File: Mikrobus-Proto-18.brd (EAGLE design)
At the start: 27.9 x 57.1 mm, 38 parts

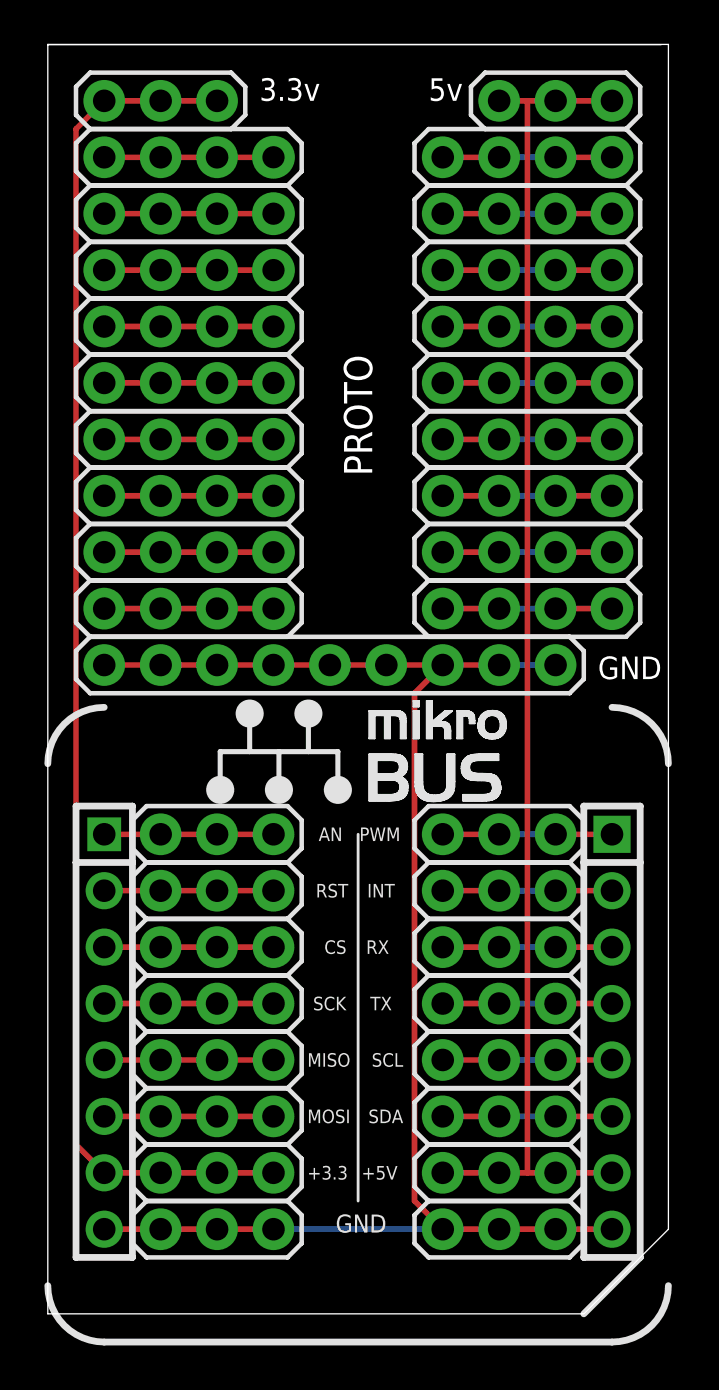
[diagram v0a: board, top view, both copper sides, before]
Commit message: Add Ground Plane
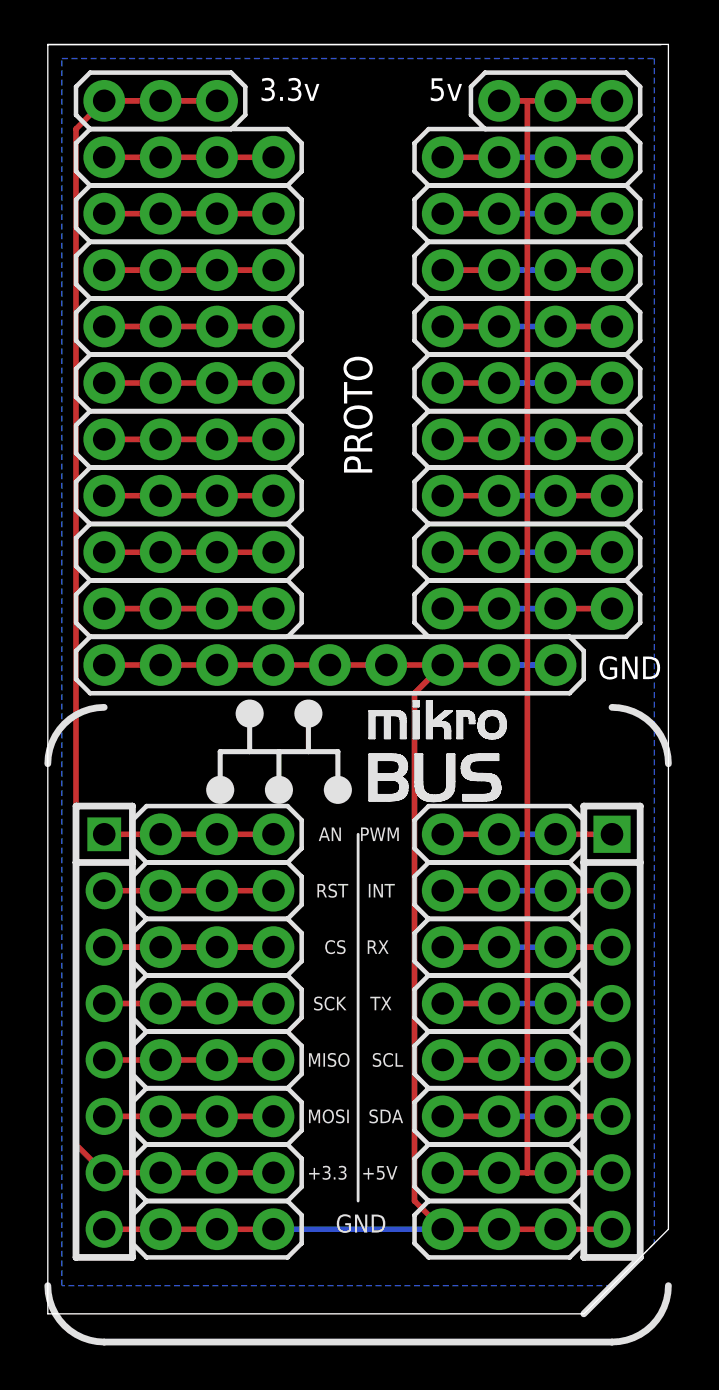
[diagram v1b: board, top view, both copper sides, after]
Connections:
- removed net N$21: JP8.1, JP8.2, JP8.3, JP9.1, JP9.2, JP9.3, MB1.8, MB1.9, U$3.1, U$3.2, U$3.3, U$3.4, U$3.5, U$3.6, U$3.7, U$3.8, U$3.9
- removed net N$46: U$18.1, U$18.2, U$18.3, U$18.4
- new net GND: JP8.1, JP8.2, JP8.3, JP9.1, JP9.2, JP9.3, MB1.8, MB1.9, U$18.1, U$18.2, U$18.3, U$18.4, U$3.1, U$3.2, U$3.3, U$3.4, U$3.5, U$3.6, U$3.7, U$3.8, U$3.9
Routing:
- net GND: track 0.00 -> 77.3 mm
- net N$21: track 69.6 -> 0.00 mm
- net N$46: track 7.62 -> 0.00 mm
- added copper zone on layer 16, net GND

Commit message: Signal names changed for preperation of Fritzing parts
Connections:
- net N$1 renamed INT
- net N$11 renamed MISO
- net N$13 renamed AN
- net N$15 renamed MOSI
- net N$2 renamed +5V
- net N$24 renamed PWM
- net N$26 renamed TX
- net N$29 renamed RX
- net N$32 renamed SDA
- net N$35 renamed SCL
- net N$4 renamed +3.3V
- net N$43 renamed RST
- net N$48 renamed SCK
- net N$5 renamed CS
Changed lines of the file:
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@@
 </elements>
 <signals>
-<signal name="N$13">
+<signal name="AN">
 <contactref element="JP1" pad="3"/>
 <contactref element="MB1" pad="1"/>
@@
 <wire x1="7.62" y1="22.86" x2="5.08" y2="22.86" width="0.254" layer="1"/>
 </signal>
-<signal name="N$1">
+<signal name="INT">
 <contactref element="JP16" pad="1"/>
 <contactref element="MB1" pad="15"/>
@@
 <wire x1="20.32" y1="20.32" x2="22.86" y2="20.32" width="0.254" layer="16"/>
 </signal>
-<signal name="N$5">
+<signal name="CS">
 <contactref element="JP3" pad="2"/>
 <contactref element="JP3" pad="1"/>
@@
 <wire x1="7.62" y1="17.78" x2="10.16" y2="17.78" width="0.254" layer="1"/>
 </signal>
-<signal name="N$11">
+<signal name="MISO">
 <contactref element="JP5" pad="2"/>
 <contactref element="JP5" pad="1"/>
@@
 <wire x1="7.62" y1="12.7" x2="10.16" y2="12.7" width="0.254" layer="1"/>
 </signal>
-<signal name="N$15">
+<signal name="MOSI">
 <contactref element="JP6" pad="2"/>
 <contactref element="JP6" pad="1"/>
@@
 <wire x1="7.62" y1="10.16" x2="10.16" y2="10.16" width="0.254" layer="1"/>
 </signal>
-<signal name="N$24">
+<signal name="PWM">
 <contactref element="JP15" pad="2"/>
 <contactref element="MB1" pad="16"/>
@@
 <wire x1="20.32" y1="22.86" x2="22.86" y2="22.86" width="0.254" layer="16"/>
 </signal>
-<signal name="N$26">
+<signal name="TX">
 <contactref element="JP13" pad="1"/>
 <contactref element="MB1" pad="13"/>
@@
 <wire x1="20.32" y1="15.24" x2="22.86" y2="15.24" width="0.254" layer="16"/>
 </signal>
-<signal name="N$29">
+<signal name="RX">
 <contactref element="JP14" pad="1"/>
 <contactref element="MB1" pad="14"/>
@@
 <wire x1="20.32" y1="17.78" x2="22.86" y2="17.78" width="0.254" layer="16"/>
 </signal>
-<signal name="N$32">
+<signal name="SDA">
 <contactref element="JP11" pad="1"/>
 <contactref element="MB1" pad="11"/>
@@
 <wire x1="20.32" y1="10.16" x2="22.86" y2="10.16" width="0.254" layer="16"/>
 </signal>
-<signal name="N$35">
+<signal name="SCL">
 <contactref element="JP12" pad="1"/>
 <contactref element="MB1" pad="12"/>
@@
 <wire x1="20.32" y1="12.7" x2="22.86" y2="12.7" width="0.254" layer="16"/>
 </signal>
-<signal name="N$4">
+<signal name="+3.3V">
 <contactref element="JP7" pad="1"/>
 <contactref element="JP17" pad="3"/>
@@
 <wire x1="22.86" y1="53.34" x2="20.32" y2="53.34" width="0.254" layer="16"/>
 </signal>
-<signal name="N$43">
+<signal name="RST">
 <contactref element="JP2" pad="1"/>
 <contactref element="JP2" pad="2"/>
@@
 <wire x1="7.62" y1="20.32" x2="10.16" y2="20.32" width="0.254" layer="1"/>
 </signal>
-<signal name="N$48">
+<signal name="SCK">
 <contactref element="JP4" pad="1"/>
 <contactref element="JP4" pad="2"/>
@@
 <wire x1="7.62" y1="15.24" x2="10.16" y2="15.24" width="0.254" layer="1"/>
 </signal>
-<signal name="N$2">
+<signal name="+5V">
 <contactref element="JP10" pad="1"/>
 <contactref element="MB1" pad="10"/>

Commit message: Better Fritzing part thanks to Steve Lilley
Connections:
- net N$12 renamed R8
- net N$16 renamed L7
- net N$17 renamed R7
- net N$19 renamed L6
- net N$20 renamed R6
- net N$22 renamed R9
- net N$25 renamed L8
- net N$28 renamed L5
- net N$31 renamed R5
- net N$34 renamed L4
- net N$37 renamed R4
- net N$38 renamed L3
- net N$40 renamed R3
- net N$44 renamed L2
- net N$45 renamed R2
- net N$47 renamed R1
- net N$9 renamed L9
- new net L1: U$18.1, U$18.2, U$18.3, U$18.4
- net GND: no longer U$18.1, U$18.2, U$18.3, U$18.4
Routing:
- net GND: track 77.3 -> 69.6 mm
- net L1: track 0.00 -> 7.62 mm
- added copper zone on layer 16, net L1
- removed copper zone on layer 16, net GND
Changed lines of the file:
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@@
 <wire x1="2.54" y1="7.62" x2="1.27" y2="8.89" width="0.254" layer="1"/>
 </signal>
-<signal name="N$9">
+<signal name="L9">
 <contactref element="U$4" pad="1"/>
 <contactref element="U$4" pad="4"/>
@@
 <wire x1="7.62" y1="33.02" x2="10.16" y2="33.02" width="0.254" layer="1"/>
 </signal>
-<signal name="N$12">
+<signal name="R8">
 <contactref element="U$7" pad="1"/>
 <contactref element="U$7" pad="4"/>
@@
 <wire x1="22.86" y1="35.56" x2="20.32" y2="35.56" width="0.254" layer="16"/>
 </signal>
-<signal name="N$16">
+<signal name="L7">
 <contactref element="U$8" pad="1"/>
 <contactref element="U$8" pad="4"/>
@@
 <wire x1="7.62" y1="38.1" x2="10.16" y2="38.1" width="0.254" layer="1"/>
 </signal>
-<signal name="N$17">
+<signal name="R7">
 <contactref element="U$9" pad="1"/>
 <contactref element="U$9" pad="4"/>
@@
 <wire x1="22.86" y1="38.1" x2="20.32" y2="38.1" width="0.254" layer="16"/>
 </signal>
-<signal name="N$19">
+<signal name="L6">
 <contactref element="U$10" pad="1"/>
 <contactref element="U$10" pad="4"/>
@@
 <wire x1="7.62" y1="40.64" x2="10.16" y2="40.64" width="0.254" layer="1"/>
 </signal>
-<signal name="N$20">
+<signal name="R6">
 <contactref element="U$11" pad="1"/>
 <contactref element="U$11" pad="4"/>
@@
 <wire x1="22.86" y1="40.64" x2="20.32" y2="40.64" width="0.254" layer="16"/>
 </signal>
-<signal name="N$22">
+<signal name="R9">
 <contactref element="U$5" pad="1"/>
 <contactref element="U$5" pad="4"/>
@@
 <wire x1="22.86" y1="33.02" x2="20.32" y2="33.02" width="0.254" layer="16"/>
 </signal>
-<signal name="N$25">
+<signal name="L8">
 <contactref element="U$6" pad="1"/>
 <contactref element="U$6" pad="4"/>
@@
 <wire x1="7.62" y1="35.56" x2="10.16" y2="35.56" width="0.254" layer="1"/>
 </signal>
-<signal name="N$28">
+<signal name="L5">
 <contactref element="U$12" pad="1"/>
 <contactref element="U$12" pad="4"/>
@@
 <wire x1="7.62" y1="43.18" x2="10.16" y2="43.18" width="0.254" layer="1"/>
 </signal>
-<signal name="N$31">
+<signal name="R5">
 <contactref element="U$13" pad="1"/>
 <contactref element="U$13" pad="4"/>
@@
 <wire x1="22.86" y1="43.18" x2="20.32" y2="43.18" width="0.254" layer="16"/>
 </signal>
-<signal name="N$34">
+<signal name="L4">
 <contactref element="U$14" pad="1"/>
 <contactref element="U$14" pad="4"/>
@@
 <wire x1="7.62" y1="45.72" x2="10.16" y2="45.72" width="0.254" layer="1"/>
 </signal>
-<signal name="N$37">
+<signal name="R4">
 <contactref element="U$15" pad="1"/>
 <contactref element="U$15" pad="4"/>
@@
 <wire x1="22.86" y1="45.72" x2="20.32" y2="45.72" width="0.254" layer="16"/>
 </signal>
-<signal name="N$38">
+<signal name="L3">
 <contactref element="U$16" pad="1"/>
 <contactref element="U$16" pad="4"/>
@@
 <wire x1="7.62" y1="48.26" x2="10.16" y2="48.26" width="0.254" layer="1"/>
 </signal>
-<signal name="N$40">
+<signal name="R3">
 <contactref element="U$17" pad="1"/>
 <contactref element="U$17" pad="4"/>
@@
 <wire x1="22.86" y1="48.26" x2="20.32" y2="48.26" width="0.254" layer="16"/>
 </signal>
-<signal name="N$44">
+<signal name="L2">
 <contactref element="U$1" pad="1"/>
 <contactref element="U$1" pad="4"/>
@@
 <wire x1="7.62" y1="50.8" x2="10.16" y2="50.8" width="0.254" layer="1"/>
 </signal>
-<signal name="N$45">
+<signal name="R2">
 <contactref element="U$2" pad="1"/>
 <contactref element="U$2" pad="4"/>
@@
 <wire x1="22.86" y1="50.8" x2="20.32" y2="50.8" width="0.254" layer="16"/>
 </signal>
-<signal name="GND">
+<signal name="L1">
 <contactref element="U$18" pad="1"/>
 <contactref element="U$18" pad="4"/>
@@
 <wire x1="5.08" y1="53.34" x2="7.62" y2="53.34" width="0.254" layer="1"/>
 <wire x1="7.62" y1="53.34" x2="10.16" y2="53.34" width="0.254" layer="1"/>
+<polygon width="0.254" layer="16">
+<vertex x="0.635" y="57.785"/>
+<vertex x="27.305" y="57.785"/>
+<vertex x="27.305" y="4.445"/>
+<vertex x="25.4" y="2.54"/>
+<vertex x="0.635" y="2.54"/>
+</polygon>
+</signal>
+<signal name="R1">
+<contactref element="U$19" pad="1"/>
+<contactref element="U$19" pad="4"/>
+<contactref element="U$19" pad="2"/>
+<contactref element="U$19" pad="3"/>
+<wire x1="20.32" y1="53.34" x2="17.78" y2="53.34" width="0.254" layer="1"/>
+<wire x1="25.4" y1="53.34" x2="22.86" y2="53.34" width="0.254" layer="1"/>
+<wire x1="22.86" y1="53.34" x2="20.32" y2="53.34" width="0.254" layer="16"/>
+</signal>
+<signal name="RST">
+<contactref element="JP2" pad="1"/>
+<contactref element="JP2" pad="2"/>
+<contactref element="JP2" pad="3"/>
+<contactref element="MB1" pad="2"/>
+<wire x1="5.08" y1="20.32" x2="2.54" y2="20.32" width="0.254" layer="1"/>
+<wire x1="5.08" y1="20.32" x2="7.62" y2="20.32" width="0.254" layer="1"/>
+<wire x1="7.62" y1="20.32" x2="10.16" y2="20.32" width="0.254" layer="1"/>
+</signal>
+<signal name="SCK">
+<contactref element="JP4" pad="1"/>
+<contactref element="JP4" pad="2"/>
+<contactref element="JP4" pad="3"/>
+<contactref element="MB1" pad="4"/>
+<wire x1="5.08" y1="15.24" x2="2.54" y2="15.24" width="0.254" layer="1"/>
+<wire x1="5.08" y1="15.24" x2="7.62" y2="15.24" width="0.254" layer="1"/>
+<wire x1="7.62" y1="15.24" x2="10.16" y2="15.24" width="0.254" layer="1"/>
+</signal>
+<signal name="+5V">
+<contactref element="JP10" pad="1"/>
+<contactref element="MB1" pad="10"/>
+<contactref element="JP10" pad="2"/>
+<contactref element="JP10" pad="3"/>
+<contactref element="JP18" pad="1"/>
+<contactref element="JP18" pad="2"/>
+<contactref element="JP18" pad="3"/>
+<wire x1="22.86" y1="55.88" x2="21.59" y2="55.88" width="0.254" layer="1"/>
+<wire x1="21.59" y1="55.88" x2="20.32" y2="55.88" width="0.254" layer="1"/>
+<wire x1="22.86" y1="55.88" x2="25.4" y2="55.88" width="0.254" layer="1"/>
+<wire x1="22.86" y1="7.62" x2="25.4" y2="7.62" width="0.254" layer="1"/>
+<wire x1="20.32" y1="7.62" x2="17.78" y2="7.62" width="0.254" layer="1"/>
+<wire x1="20.32" y1="7.62" x2="21.59" y2="7.62" width="0.254" layer="1"/>
+<wire x1="21.59" y1="7.62" x2="22.86" y2="7.62" width="0.254" layer="1"/>
+<wire x1="21.59" y1="7.62" x2="21.59" y2="55.88" width="0.254" layer="1"/>
+</signal>
+<signal name="GND">
 <contactref element="JP8" pad="2"/>
 <contactref element="JP8" pad="1"/>
@@
 <wire x1="16.51" y1="6.35" x2="16.51" y2="29.21" width="0.254" layer="1"/>
 <wire x1="17.78" y1="5.08" x2="16.51" y2="6.35" width="0.254" layer="1"/>
-<wire x1="2.54" y1="30.48" x2="2.54" y2="53.34" width="0" layer="19" extent="1-1"/>
-<polygon width="0.254" layer="16">
-<vertex x="0.635" y="57.785"/>
-<vertex x="27.305" y="57.785"/>
-<vertex x="27.305" y="4.445"/>
-<vertex x="25.4" y="2.54"/>
-<vertex x="0.635" y="2.54"/>
-</polygon>
-</signal>
-<signal name="N$47">
-<contactref element="U$19" pad="1"/>
-<contactref element="U$19" pad="4"/>
-<contactref element="U$19" pad="2"/>
-<contactref element="U$19" pad="3"/>
-<wire x1="20.32" y1="53.34" x2="17.78" y2="53.34" width="0.254" layer="1"/>
-<wire x1="25.4" y1="53.34" x2="22.86" y2="53.34" width="0.254" layer="1"/>
-<wire x1="22.86" y1="53.34" x2="20.32" y2="53.34" width="0.254" layer="16"/>
-</signal>
-<signal name="RST">
-<contactref element="JP2" pad="1"/>
-<contactref element="JP2" pad="2"/>
-<contactref element="JP2" pad="3"/>
-<contactref element="MB1" pad="2"/>
-<wire x1="5.08" y1="20.32" x2="2.54" y2="20.32" width="0.254" layer="1"/>
-<wire x1="5.08" y1="20.32" x2="7.62" y2="20.32" width="0.254" layer="1"/>
-<wire x1="7.62" y1="20.32" x2="10.16" y2="20.32" width="0.254" layer="1"/>
-</signal>
-<signal name="SCK">
-<contactref element="JP4" pad="1"/>
-<contactref element="JP4" pad="2"/>
-<contactref element="JP4" pad="3"/>
-<contactref element="MB1" pad="4"/>
-<wire x1="5.08" y1="15.24" x2="2.54" y2="15.24" width="0.254" layer="1"/>
-<wire x1="5.08" y1="15.24" x2="7.62" y2="15.24" width="0.254" layer="1"/>
-<wire x1="7.62" y1="15.24" x2="10.16" y2="15.24" width="0.254" layer="1"/>
-</signal>
-<signal name="+5V">
-<contactref element="JP10" pad="1"/>
-<contactref element="MB1" pad="10"/>
-<contactref element="JP10" pad="2"/>
-<contactref element="JP10" pad="3"/>
-<contactref element="JP18" pad="1"/>
-<contactref element="JP18" pad="2"/>
-<contactref element="JP18" pad="3"/>
-<wire x1="22.86" y1="55.88" x2="21.59" y2="55.88" width="0.254" layer="1"/>
-<wire x1="21.59" y1="55.88" x2="20.32" y2="55.88" width="0.254" layer="1"/>
-<wire x1="22.86" y1="55.88" x2="25.4" y2="55.88" width="0.254" layer="1"/>
-<wire x1="22.86" y1="7.62" x2="25.4" y2="7.62" width="0.254" layer="1"/>
-<wire x1="20.32" y1="7.62" x2="17.78" y2="7.62" width="0.254" layer="1"/>
-<wire x1="20.32" y1="7.62" x2="21.59" y2="7.62" width="0.254" layer="1"/>
-<wire x1="21.59" y1="7.62" x2="22.86" y2="7.62" width="0.254" layer="1"/>
-<wire x1="21.59" y1="7.62" x2="21.59" y2="55.88" width="0.254" layer="1"/>
 </signal>
 </signals>
